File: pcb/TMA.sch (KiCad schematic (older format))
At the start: 22 parts, among them J1 Conn_01x02, U1 BMP280, U2 BMI160, U3 ATtiny1614-SS, U4 MIC5504-3.3YM5

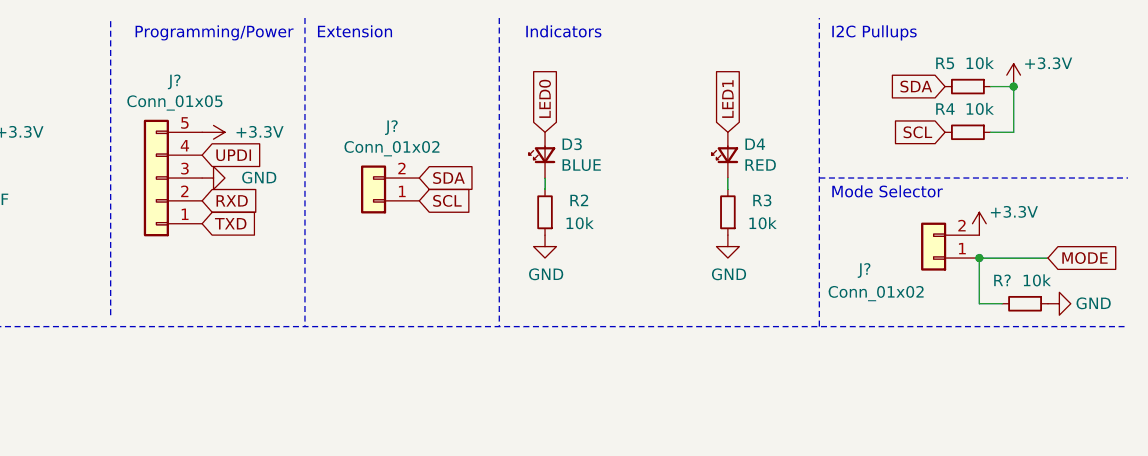
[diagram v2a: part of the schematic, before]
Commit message: Simplify, add voltage to extension.
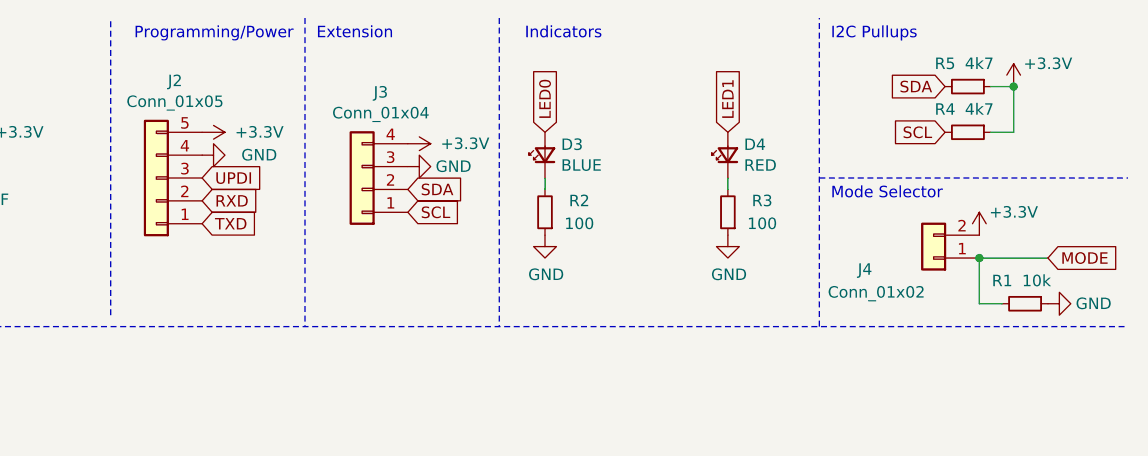
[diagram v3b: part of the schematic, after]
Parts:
- removed J?: Conn_01x02, symbol Connector_Generic:Conn_01x02
- added J3: Conn_01x04, Connector_JST:JST_PH_S4B-PH-K_1x04_P2.00mm_Horizontal, symbol Connector_Generic:Conn_01x04
- J1: footprint Connector_JST:JST_PH_B2B-PH-K_1x02_P2.00mm_Vertical -> Connector_JST:JST_PH_S2B-PH-K_1x02_P2.00mm_Horizontal
- J2: renamed from J?; footprint (none) -> Connector_JST:JST_PH_S5B-PH-K_1x05_P2.00mm_Horizontal
- J4: renamed from J?; footprint (none) -> Connector_JST:JST_PH_S2B-PH-K_1x02_P2.00mm_Horizontal
- R2, R3: value 10k -> 100
- R4, R5: value 10k -> 4k7
- gave numbers to parts that had none: 1
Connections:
- net +3V3: now also J3.4 (Pin_4)
- net GND: now also J2.4 (Pin_4), J3.3 (Pin_3); no longer J2.3 (Pin_3)
- net SCL: now also J3.1 (Pin_1)
- net SDA: now also J3.2 (Pin_2)
- net UPDI: now also J2.3 (Pin_3); no longer J2.4 (Pin_4)
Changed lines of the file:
@@
 F 0 "J1" H 2818 775 50  0000 C CNN
 F 1 "Conn_01x02" H 2818 866 50  0000 C CNN
-F 2 "Connector_JST:JST_PH_B2B-PH-K_1x02_P2.00mm_Vertical" H 2900 1100 50  0001 C CNN
+F 2 "Connector_JST:JST_PH_S2B-PH-K_1x02_P2.00mm_Horizontal" H 2900 1100 50  0001 C CNN
 F 3 "~" H 2900 1100 50  0001 C CNN
 	1    2900 1100
@@
 L power:GND #PWR012
 U 1 1 607C2610
-P 7150 1200
-F 0 "#PWR012" H 7150 950 50  0001 C CNN
-F 1 "GND" V 7150 950 50  0000 C CNN
-F 2 "" H 7150 1200 50  0001 C CNN
-F 3 "" H 7150 1200 50  0001 C CNN
-	1    7150 1200
+P 7150 1100
+F 0 "#PWR012" H 7150 850 50  0001 C CNN
+F 1 "GND" V 7150 850 50  0000 C CNN
+F 2 "" H 7150 1100 50  0001 C CNN
+F 3 "" H 7150 1100 50  0001 C CNN
+	1    7150 1100
 	0    -1   -1   0
 $EndComp
-Text GLabel 7150 1100 2    50   Input ~ 0
+Text GLabel 7150 1200 2    50   Input ~ 0
 UPDI
 Wire Notes Line
@@
 P 8650 1350
 F 0 "R2" H 8500 1300 50  0000 C CNN
-F 1 "10k" H 8500 1400 50  0000 C CNN
+F 1 "100" H 8500 1400 50  0000 C CNN
 F 2 "Resistor_SMD:R_0402_1005Metric" H 8650 1350 50  0001 C CNN
 F 3 "~" H 8650 1350 50  0001 C CNN
@@
 P 9450 1350
 F 0 "R3" H 9300 1300 50  0000 C CNN
-F 1 "10k" H 9300 1400 50  0000 C CNN
+F 1 "100" H 9300 1400 50  0000 C CNN
 F 2 "Resistor_SMD:R_0402_1005Metric" H 9450 1350 50  0001 C CNN
 F 3 "~" H 9450 1350 50  0001 C CNN
@@
 P 10500 1000
 F 0 "R4" V 10400 900 50  0000 C CNN
-F 1 "10k" V 10400 1050 50  0000 C CNN
+F 1 "4k7" V 10400 1050 50  0000 C CNN
 F 2 "Resistor_SMD:R_0402_1005Metric" H 10500 1000 50  0001 C CNN
 F 3 "~" H 10500 1000 50  0001 C CNN
@@
 P 10500 800
 F 0 "R5" V 10400 700 50  0000 C CNN
-F 1 "10k" V 10400 850 50  0000 C CNN
+F 1 "4k7" V 10400 850 50  0000 C CNN
 F 2 "Resistor_SMD:R_0402_1005Metric" H 10500 800 50  0001 C CNN
 F 3 "~" H 10500 800 50  0001 C CNN
@@
 	4300 1000 4350 1000
 $Comp
-L Connector_Generic:Conn_01x05 J?
+L Connector_Generic:Conn_01x05 J2
 U 1 1 607DB715
 P 6950 1200
-F 0 "J?" H 6868 775 50  0000 C CNN
+F 0 "J2" H 6868 775 50  0000 C CNN
 F 1 "Conn_01x05" H 6868 866 50  0000 C CNN
-F 2 "" H 6950 1200 50  0001 C CNN
+F 2 "Connector_JST:JST_PH_S5B-PH-K_1x05_P2.00mm_Horizontal" H 6950 1200 50  0001 C CNN
 F 3 "~" H 6950 1200 50  0001 C CNN
 	1    6950 1200
@@
 Text Notes 7650 600  0    50   ~ 0
 Extension
-$Comp
-L Connector_Generic:Conn_01x02 J?
-U 1 1 607EE0F5
-P 7900 1300
-F 0 "J?" H 7818 975 50  0000 C CNN
-F 1 "Conn_01x02" H 7818 1066 50  0000 C CNN
-F 2 "" H 7900 1300 50  0001 C CNN
-F 3 "~" H 7900 1300 50  0001 C CNN
-	1    7900 1300
-	-1   0    0    1
-$EndComp
-Text GLabel 8100 1200 2    50   Input ~ 0
+Text GLabel 8050 1250 2    50   Input ~ 0
 SDA
-Text GLabel 8100 1300 2    50   Input ~ 0
+Text GLabel 8050 1350 2    50   Input ~ 0
 SCL
 Text GLabel 10850 1550 2    50   Input ~ 0
@@
 Mode Selector
 $Comp
-L Connector_Generic:Conn_01x02 J?
+L Connector_Generic:Conn_01x02 J4
 U 1 1 607F369F
 P 10350 1550
-F 0 "J?" H 10650 1600 50  0000 C CNN
+F 0 "J4" H 10650 1600 50  0000 C CNN
 F 1 "Conn_01x02" H 10600 1700 50  0000 C CNN
-F 2 "" H 10350 1550 50  0001 C CNN
+F 2 "Connector_JST:JST_PH_S2B-PH-K_1x02_P2.00mm_Horizontal" H 10350 1550 50  0001 C CNN
 F 3 "~" H 10350 1550 50  0001 C CNN
 	1    10350 1550
@@
 $EndComp
 $Comp
-L power:+3.3V #PWR?
+L power:+3.3V #PWR018
 U 1 1 607F6852
 P 10550 1450
-F 0 "#PWR?" H 10550 1300 50  0001 C CNN
+F 0 "#PWR018" H 10550 1300 50  0001 C CNN
 F 1 "+3.3V" H 10700 1550 50  0000 C CNN
 F 2 "" H 10550 1450 50  0001 C CNN
@@
 $EndComp
 $Comp
-L Device:R_Small R?
+L Device:R_Small R1
 U 1 1 607F6F0C
 P 10750 1750
-F 0 "R?" V 10650 1650 50  0000 C CNN
+F 0 "R1" V 10650 1650 50  0000 C CNN
 F 1 "10k" V 10650 1800 50  0000 C CNN
 F 2 "Resistor_SMD:R_0402_1005Metric" H 10750 1750 50  0001 C CNN
@@
 $EndComp
 $Comp
-L power:GND #PWR?
+L power:GND #PWR019
 U 1 1 607F7A49
 P 10850 1750
-F 0 "#PWR?" H 10850 1500 50  0001 C CNN
+F 0 "#PWR019" H 10850 1500 50  0001 C CNN
 F 1 "GND" V 10850 1550 50  0000 C CNN
 F 2 "" H 10850 1750 50  0001 C CNN
@@
 	10550 1550 10850 1550
 Connection ~ 10550 1550
+$Comp
+L Connector_Generic:Conn_01x04 J3
+U 1 1 6079D0A1
+P 7850 1250
+F 0 "J3" H 7768 825 50  0000 C CNN
+F 1 "Conn_01x04" H 7768 916 50  0000 C CNN
+F 2 "Connector_JST:JST_PH_S4B-PH-K_1x04_P2.00mm_Horizontal" H 7850 1250 50  0001 C CNN
+F 3 "~" H 7850 1250 50  0001 C CNN
+	1    7850 1250
+	-1   0    0    1
+$EndComp
+$Comp
+L power:+3.3V #PWR015
+U 1 1 6079DBF9
+P 8050 1050
+F 0 "#PWR015" H 8050 900 50  0001 C CNN
+F 1 "+3.3V" V 8050 1300 50  0000 C CNN
+F 2 "" H 8050 1050 50  0001 C CNN
+F 3 "" H 8050 1050 50  0001 C CNN
+	1    8050 1050
+	0    1    1    0
+$EndComp
+$Comp
+L power:GND #PWR016
+U 1 1 6079DFC3
+P 8050 1150
+F 0 "#PWR016" H 8050 900 50  0001 C CNN
+F 1 "GND" V 8050 950 50  0000 C CNN
+F 2 "" H 8050 1150 50  0001 C CNN
+F 3 "" H 8050 1150 50  0001 C CNN
+	1    8050 1150
+	0    -1   -1   0
+$EndComp
 $EndSCHEMATC

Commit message: Routing!
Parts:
- J1, J4: footprint Connector_JST:JST_PH_S2B-PH-K_1x02_P2.00mm_Horizontal -> Connector_PinHeader_1.00mm:PinHeader_1x02_P1.00mm_Vertical_SMD_Pin1Left
- J2: footprint Connector_JST:JST_PH_S5B-PH-K_1x05_P2.00mm_Horizontal -> Connector_PinHeader_1.00mm:PinHeader_1x05_P1.00mm_Vertical_SMD_Pin1Left
- J3: footprint Connector_JST:JST_PH_S4B-PH-K_1x04_P2.00mm_Horizontal -> Connector_PinHeader_1.00mm:PinHeader_1x04_P1.00mm_Vertical_SMD_Pin1Left
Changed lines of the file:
@@
 F 0 "J1" H 2818 775 50  0000 C CNN
 F 1 "Conn_01x02" H 2818 866 50  0000 C CNN
-F 2 "Connector_JST:JST_PH_S2B-PH-K_1x02_P2.00mm_Horizontal" H 2900 1100 50  0001 C CNN
+F 2 "Connector_PinHeader_1.00mm:PinHeader_1x02_P1.00mm_Vertical_SMD_Pin1Left" H 2900 1100 50  0001 C CNN
 F 3 "~" H 2900 1100 50  0001 C CNN
 	1    2900 1100
@@
 F 0 "J2" H 6868 775 50  0000 C CNN
 F 1 "Conn_01x05" H 6868 866 50  0000 C CNN
-F 2 "Connector_JST:JST_PH_S5B-PH-K_1x05_P2.00mm_Horizontal" H 6950 1200 50  0001 C CNN
+F 2 "Connector_PinHeader_1.00mm:PinHeader_1x05_P1.00mm_Vertical_SMD_Pin1Left" H 6950 1200 50  0001 C CNN
 F 3 "~" H 6950 1200 50  0001 C CNN
 	1    6950 1200
@@
 F 0 "J4" H 10650 1600 50  0000 C CNN
 F 1 "Conn_01x02" H 10600 1700 50  0000 C CNN
-F 2 "Connector_JST:JST_PH_S2B-PH-K_1x02_P2.00mm_Horizontal" H 10350 1550 50  0001 C CNN
+F 2 "Connector_PinHeader_1.00mm:PinHeader_1x02_P1.00mm_Vertical_SMD_Pin1Left" H 10350 1550 50  0001 C CNN
 F 3 "~" H 10350 1550 50  0001 C CNN
 	1    10350 1550
@@
 F 0 "J3" H 7768 825 50  0000 C CNN
 F 1 "Conn_01x04" H 7768 916 50  0000 C CNN
-F 2 "Connector_JST:JST_PH_S4B-PH-K_1x04_P2.00mm_Horizontal" H 7850 1250 50  0001 C CNN
+F 2 "Connector_PinHeader_1.00mm:PinHeader_1x04_P1.00mm_Vertical_SMD_Pin1Left" H 7850 1250 50  0001 C CNN
 F 3 "~" H 7850 1250 50  0001 C CNN
 	1    7850 1250
